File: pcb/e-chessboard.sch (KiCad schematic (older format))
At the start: 0 parts

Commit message: feature(kicad): adding footprint
Adding new symbol for NCV7680 and AOZ1280.
Adding new footprint for 20/15 electromaget (not finished yet).
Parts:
- added U?: AOZ1280, Package_TO_SOT_SMD:SOT-23-6, symbol lib:AOZ1280
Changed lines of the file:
@@
 Comment4 ""
 $EndDescr
+$Comp
+L lib:AOZ1280 U?
+U 1 1 5E58F9CB
+P 2750 2050
+F 0 "U?" H 2750 2375 50  0000 C CNN
+F 1 "AOZ1280" H 2750 2284 50  0000 C CNN
+F 2 "Package_TO_SOT_SMD:SOT-23-6" H 2750 2150 50  0001 C CNN
+F 3 "" H 2750 2150 50  0001 C CNN
+	1    2750 2050
+	1    0    0    -1
+$EndComp
 $EndSCHEMATC

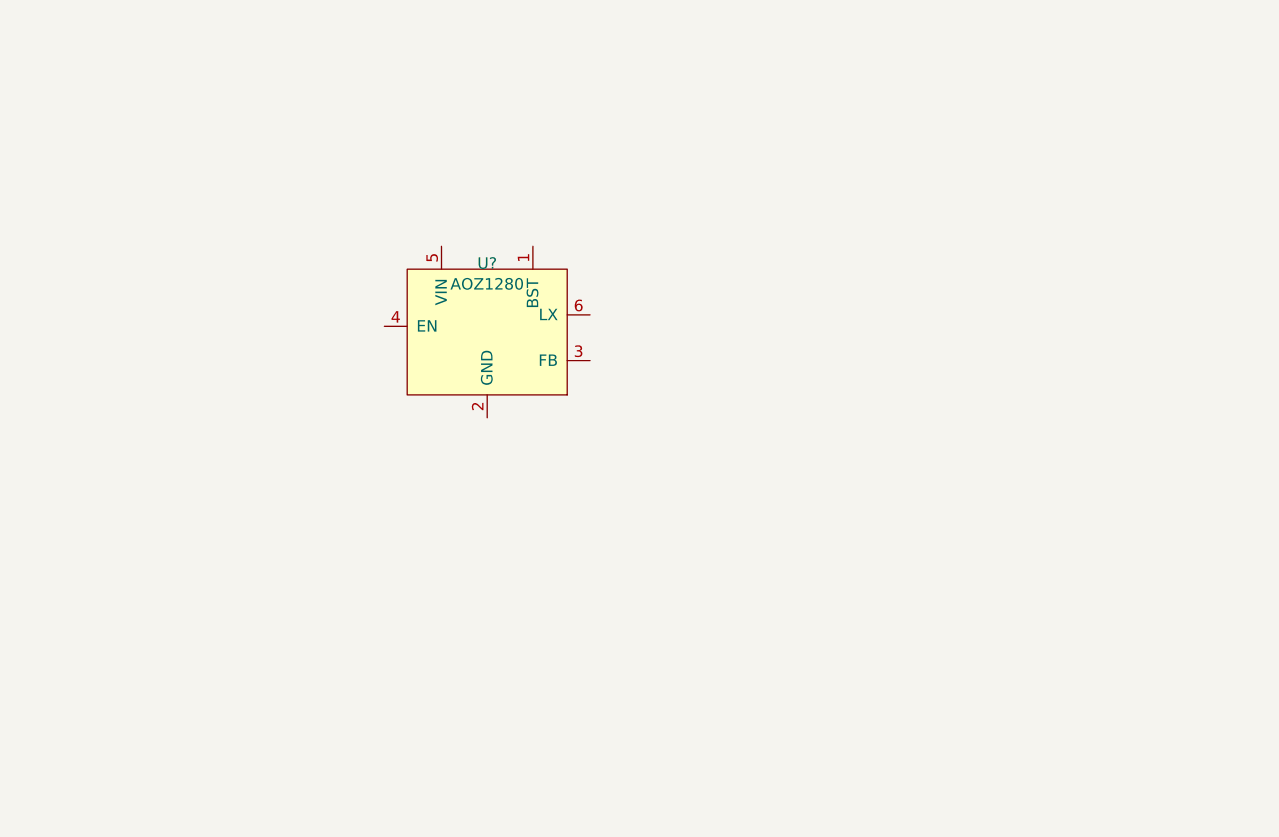
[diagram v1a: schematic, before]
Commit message: feat(kicad): adding power circuit
Adding easy power supply with capacitors. Reverse diode is missing..
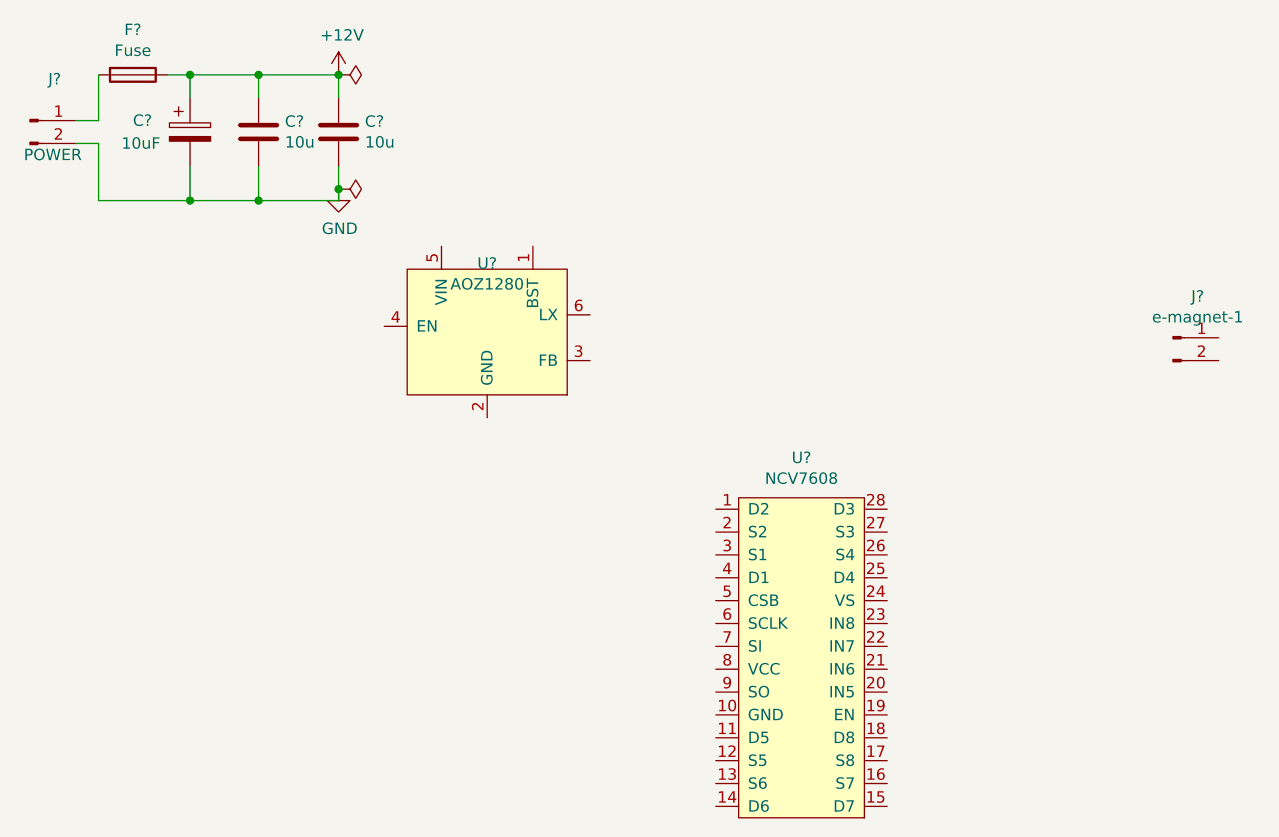
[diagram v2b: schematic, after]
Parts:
- added C? (x2): 10u, symbol Device:C
- added C?: 10uF, symbol Device:CP
- added F?: Fuse, symbol Device:Fuse
- added J?: e-magnet-1, lib_fp:20_15_electromagnet, symbol Connector:Conn_01x02_Male
- added J?: POWER, symbol Connector:Conn_01x02_Male
- added U?: NCV7608, Package_SO:SOIC-28W_7.5x17.9mm_P1.27mm, symbol lib:NCV7608
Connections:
- new net: F?.2, J?.1 (Pin_1)
- new net +12V: C?.1, C?.1, C?.1, F?.1
- new net GND: C?.2, C?.2, C?.2, J?.2 (Pin_2)
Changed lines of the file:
@@
 	1    0    0    -1
 $EndComp
+$Comp
+L lib:NCV7608 U?
+U 1 1 5E5912F6
+P 4100 3450
+F 0 "U?" H 4125 4325 50  0000 C CNN
+F 1 "NCV7608" H 4125 4234 50  0000 C CNN
+F 2 "Package_SO:SOIC-28W_7.5x17.9mm_P1.27mm" H 3900 4000 50  0001 C CNN
+F 3 "" H 3900 4000 50  0001 C CNN
+	1    4100 3450
+	1    0    0    -1
+$EndComp
+$Comp
+L Connector:Conn_01x02_Male J?
+U 1 1 5E594613
+P 5750 2050
+F 0 "J?" H 5858 2231 50  0000 C CNN
+F 1 "e-magnet-1" H 5858 2140 50  0000 C CNN
+F 2 "lib_fp:20_15_electromagnet" H 5750 2050 50  0001 C CNN
+F 3 "~" H 5750 2050 50  0001 C CNN
+	1    5750 2050
+	1    0    0    -1
+$EndComp
+$Comp
+L Device:Fuse F?
+U 1 1 5E594AB1
+P 1200 900
+F 0 "F?" V 1003 900 50  0000 C CNN
+F 1 "Fuse" V 1094 900 50  0000 C CNN
+F 2 "" V 1130 900 50  0001 C CNN
+F 3 "~" H 1200 900 50  0001 C CNN
+	1    1200 900
+	0    1    1    0
+$EndComp
+$Comp
+L Connector:Conn_01x02_Male J?
+U 1 1 5E595146
+P 750 1100
+F 0 "J?" H 858 1281 50  0000 C CNN
+F 1 "POWER" H 850 950 50  0000 C CNN
+F 2 "" H 750 1100 50  0001 C CNN
+F 3 "~" H 750 1100 50  0001 C CNN
+	1    750  1100
+	1    0    0    -1
+$EndComp
+$Comp
+L Device:C C?
+U 1 1 5E599752
+P 1750 1150
+F 0 "C?" H 1865 1196 50  0000 L CNN
+F 1 "10u" H 1865 1105 50  0000 L CNN
+F 2 "" H 1788 1000 50  0001 C CNN
+F 3 "~" H 1750 1150 50  0001 C CNN
+	1    1750 1150
+	1    0    0    -1
+$EndComp
+$Comp
+L Device:CP C?
+U 1 1 5E599FB4
+P 1450 1150
+F 0 "C?" H 1200 1200 50  0000 L CNN
+F 1 "10uF" H 1150 1100 50  0000 L CNN
+F 2 "" H 1488 1000 50  0001 C CNN
+F 3 "~" H 1450 1150 50  0001 C CNN
+	1    1450 1150
+	1    0    0    -1
+$EndComp
+$Comp
+L Device:C C?
+U 1 1 5E59B30B
+P 2100 1150
+F 0 "C?" H 2215 1196 50  0000 L CNN
+F 1 "10u" H 2215 1105 50  0000 L CNN
+F 2 "" H 2138 1000 50  0001 C CNN
+F 3 "~" H 2100 1150 50  0001 C CNN
+	1    2100 1150
+	1    0    0    -1
+$EndComp
+Wire Wire Line
+	1350 900  1450 900
+Wire Wire Line
+	2100 900  2100 1000
+Wire Wire Line
+	1750 1000 1750 900
+Connection ~ 1750 900
+Wire Wire Line
+	1750 900  2100 900
+Wire Wire Line
+	1450 1000 1450 900
+Connection ~ 1450 900
+Wire Wire Line
+	1450 900  1750 900
+$Comp
+L power:+12V #PWR?
+U 1 1 5E5A0DB1
+P 2100 900
+F 0 "#PWR?" H 2100 750 50  0001 C CNN
+F 1 "+12V" H 2115 1073 50  0000 C CNN
+F 2 "" H 2100 900 50  0001 C CNN
+F 3 "" H 2100 900 50  0001 C CNN
+	1    2100 900
+	1    0    0    -1
+$EndComp
+Connection ~ 2100 900
+$Comp
+L power:GND #PWR?
+U 1 1 5E5A132A
+P 2100 1400
+F 0 "#PWR?" H 2100 1150 50  0001 C CNN
+F 1 "GND" H 2105 1227 50  0000 C CNN
+F 2 "" H 2100 1400 50  0001 C CNN
+F 3 "" H 2100 1400 50  0001 C CNN
+	1    2100 1400
+	1    0    0    -1
+$EndComp
+$Comp
+L power:PWR_FLAG #FLG?
+U 1 1 5E5A173E
+P 2100 1400
+F 0 "#FLG?" H 2100 1475 50  0001 C CNN
+F 1 "PWR_FLAG" V 2100 1528 50  0001 L CNN
+F 2 "" H 2100 1400 50  0001 C CNN
+F 3 "~" H 2100 1400 50  0001 C CNN
+	1    2100 1400
+	0    1    1    0
+$EndComp
+$Comp
+L power:PWR_FLAG #FLG?
+U 1 1 5E5A1BD1
+P 2100 900
+F 0 "#FLG?" H 2100 975 50  0001 C CNN
+F 1 "PWR_FLAG" V 2100 1028 50  0001 L CNN
+F 2 "" H 2100 900 50  0001 C CNN
+F 3 "~" H 2100 900 50  0001 C CNN
+	1    2100 900
+	0    1    1    0
+$EndComp
+Wire Wire Line
+	2100 1300 2100 1400
+Wire Wire Line
+	2100 1450 1750 1450
+Connection ~ 2100 1400
+Wire Wire Line
+	2100 1400 2100 1450
+Wire Wire Line
+	1450 1300 1450 1450
+Connection ~ 1450 1450
+Wire Wire Line
+	1450 1450 1050 1450
+Wire Wire Line
+	1750 1300 1750 1450
+Connection ~ 1750 1450
+Wire Wire Line
+	1750 1450 1450 1450
+Wire Wire Line
+	1050 1450 1050 1200
+Wire Wire Line
+	1050 1200 950  1200
+Wire Wire Line
+	950  1100 1050 1100
+Wire Wire Line
+	1050 1100 1050 900
 $EndSCHEMATC

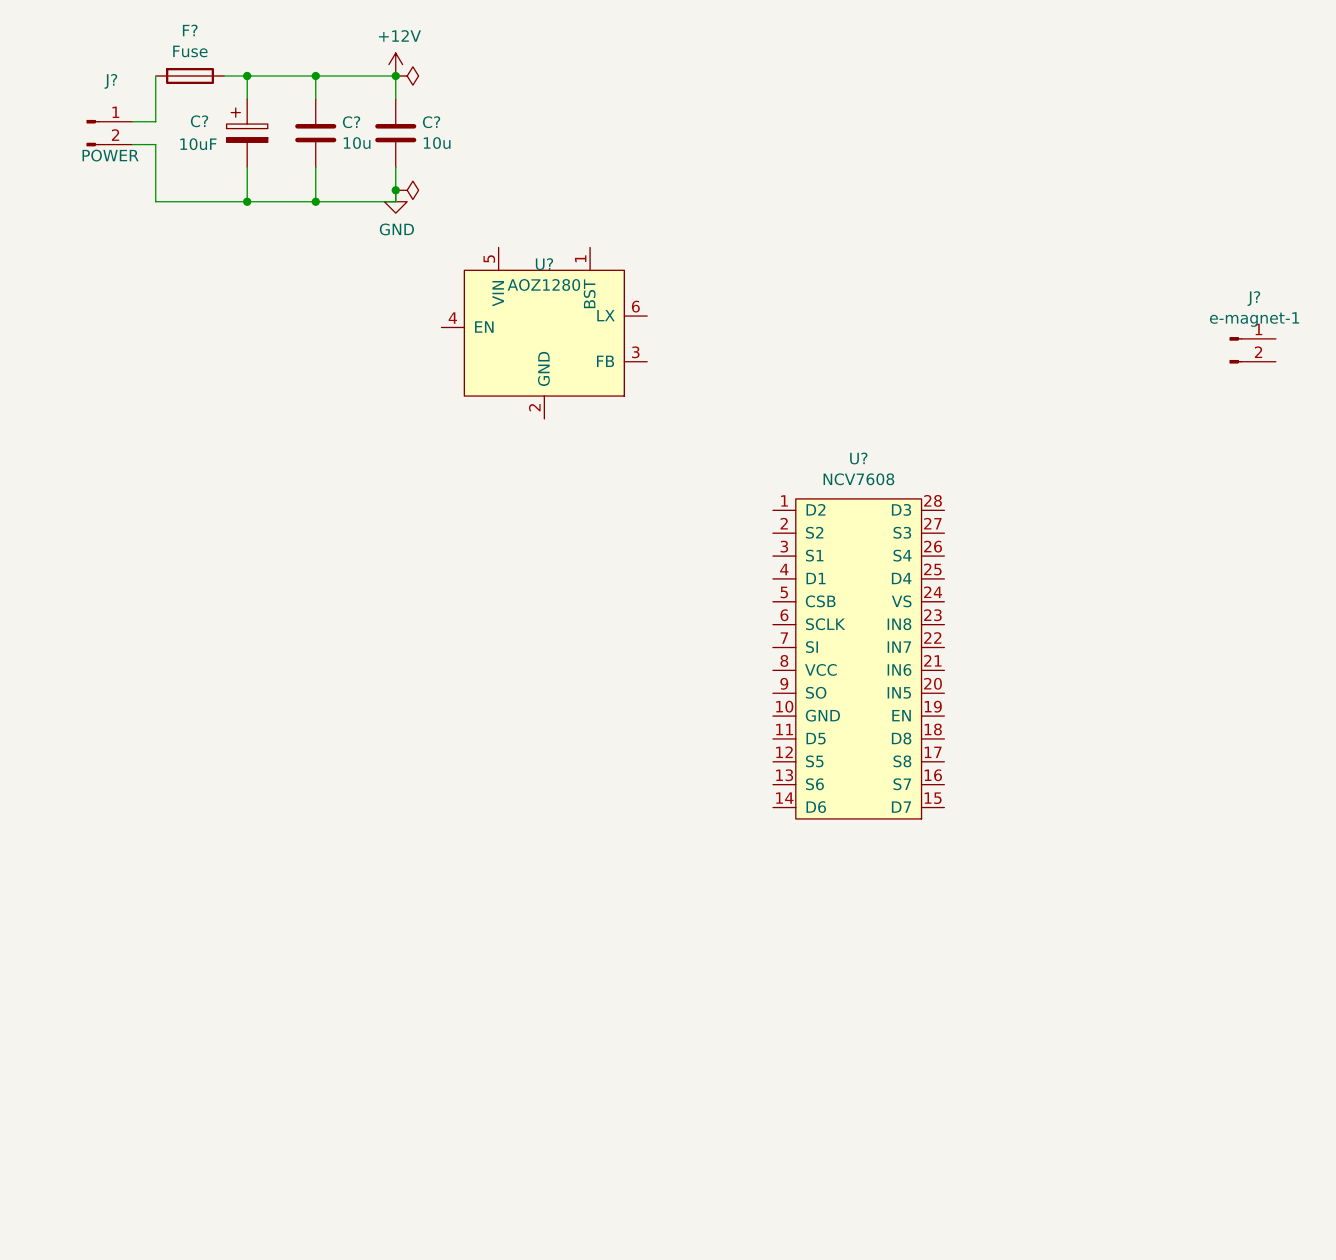
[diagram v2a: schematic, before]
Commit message: feat(kicad): adding buck converter
Adding AOZ1280 buck converter to convert 12V to 3.3V.
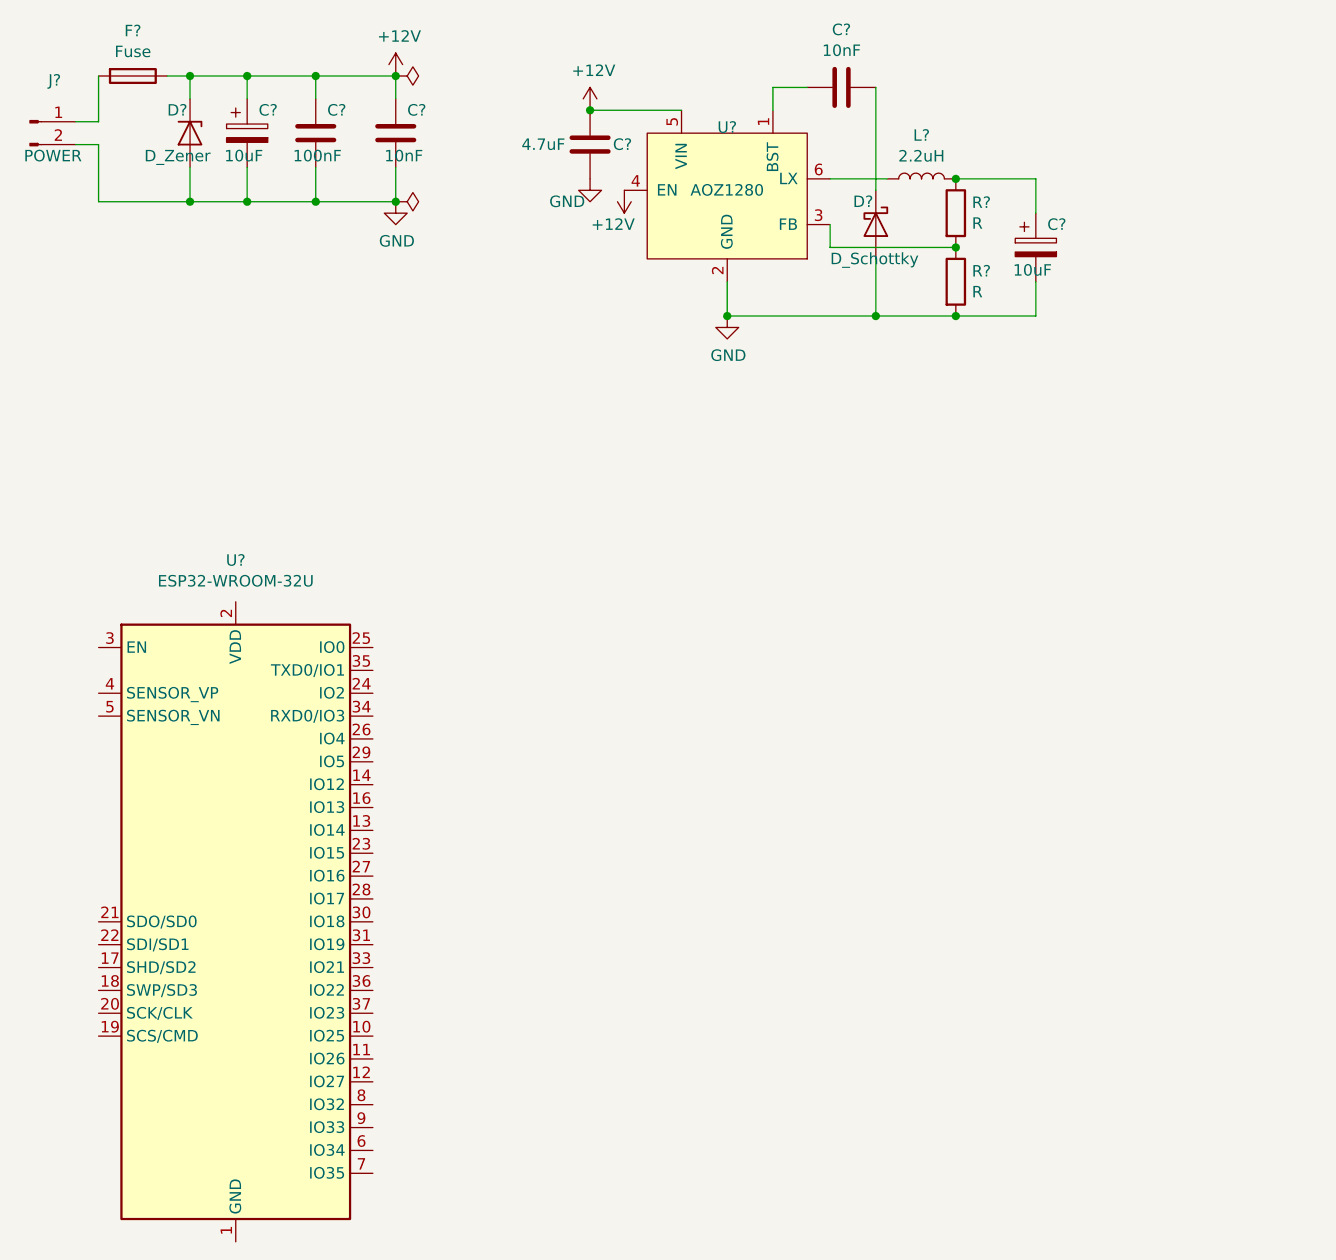
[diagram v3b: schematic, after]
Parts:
- removed J?: e-magnet-1, lib_fp:20_15_electromagnet, symbol Connector:Conn_01x02_Male
- removed U?: NCV7608, Package_SO:SOIC-28W_7.5x17.9mm_P1.27mm, symbol lib:NCV7608
- added C?: 4.7uF, symbol Device:C
- added C?: 10nF, symbol Device:C
- added C?: 10uF, symbol Device:CP
- added D?: D_Schottky, symbol Device:D_Schottky
- added D?: D_Zener, symbol Device:D_Zener
- added L?: 2.2uH, symbol Device:L
- added R? (x2): R, symbol Device:R
- added U?: ESP32-WROOM-32U, RF_Module:ESP32-WROOM-32U, symbol RF_Module:ESP32-WROOM-32U
- C?: value 10u -> 100nF
- C?: value 10u -> 10nF
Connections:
- net +12V: now also U?.4 (EN), U?.5 (VIN), C?.1, D?.1 (K)
- net GND: now also U?.2 (GND), C?.2, C?.2, D?.2 (A), D?.2 (A), R?.2
- net at U?.1 (BST): now also C?.2
- net at U?.3 (FB): now also R?.1, R?.2
- net at U?.6 (LX): now also L?.1
- new net: U?.1 (GND), U?.15 (GND), U?.38 (GND), U?.39 (GND)
- new net: C?.1, D?.1 (K)
- new net: C?.1, L?.2, R?.1
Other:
- moved on the sheet: F?, J?, U?
